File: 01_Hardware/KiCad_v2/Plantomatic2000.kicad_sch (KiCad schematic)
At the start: 256 parts, among them J101 Conn_02x05_Odd_Even, J102 Conn_02x03_Odd_Even, J103 USB_C_Receptacle_USB2.0_16P, J105 JST_B4B, J106 JST_B2B, J107 JST_B2B, J108 JST_B2B, J109 JST_B2B, J110 JST_B4B, J111 JST_B2B, J112 JST_B2B, J113 JST_B2B, J114 JST_B2B, J115 JST_B2B, J117 JST_B2B, Q101 STN3NF06L, Q102 STN3NF06L, Q103 UNH3N, Q104 BSS314PE, Q105 BSS314PE, Q106 BSS314PE, Q107 BSS314PE, Q108 NVTA7002NT1G, Q109 NVTA7002NT1G, Q110 NVTA7002NT1G, Q111 DMP6050SSD, Q112 DMP6050SSD, Q113 SI7615DN-T1-GE3, Q114 SI7615DN-T1-GE3, Q115 NVTA7002NT1G, Q116 NVTA7002NT1G, Q117 NVTA7002NT1G, SW102 SW_Push, SW103 SW_Push, U100 TLV61048, U101 XC6220B331MR, U102 BDJ2FC0WFP, U103 ESP32-WROOM-32E, U104 CYPD3177-24LQ, U105 USBLC6-2P6, U106 CP2102N-A02-GQFN24, U107 DS3231M, U108 AT24CS01-SSHM, U109 NCP1117-12_SOT223, U110 BQ25892, U111 XC6220B331MR

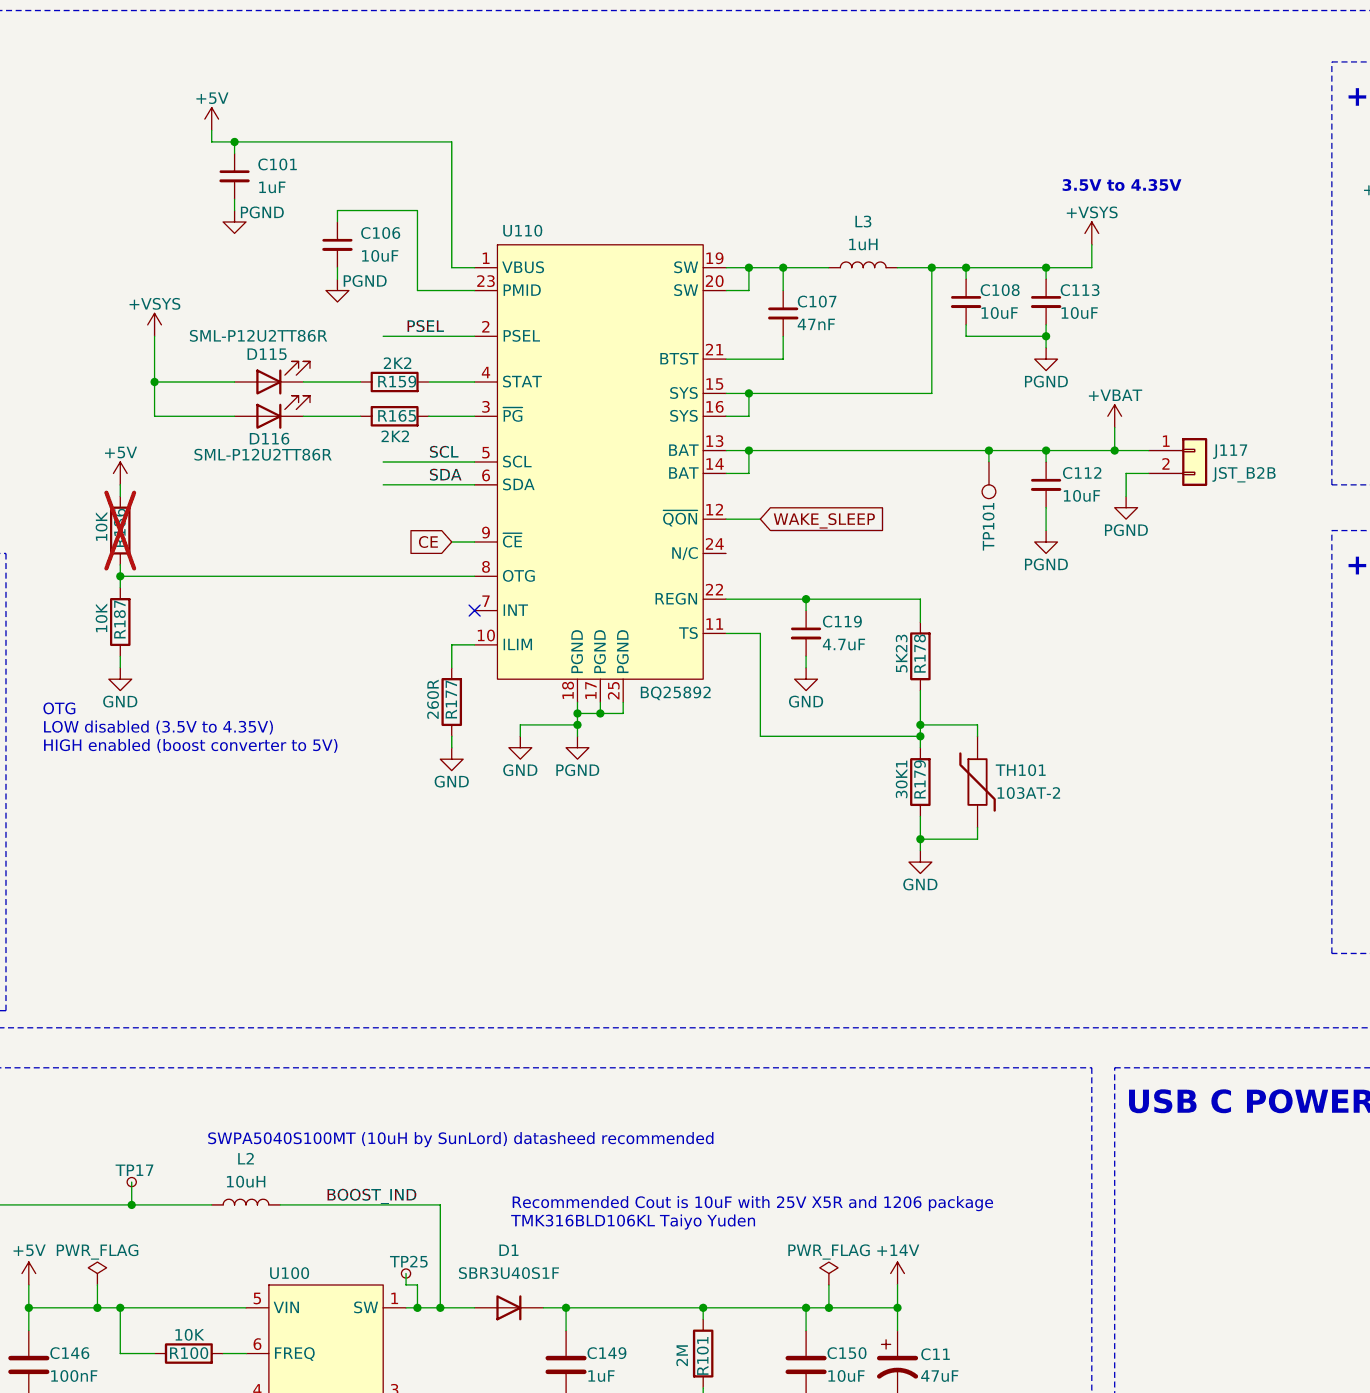
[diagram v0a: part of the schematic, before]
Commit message: Added footrpints for inductors and boost convereter
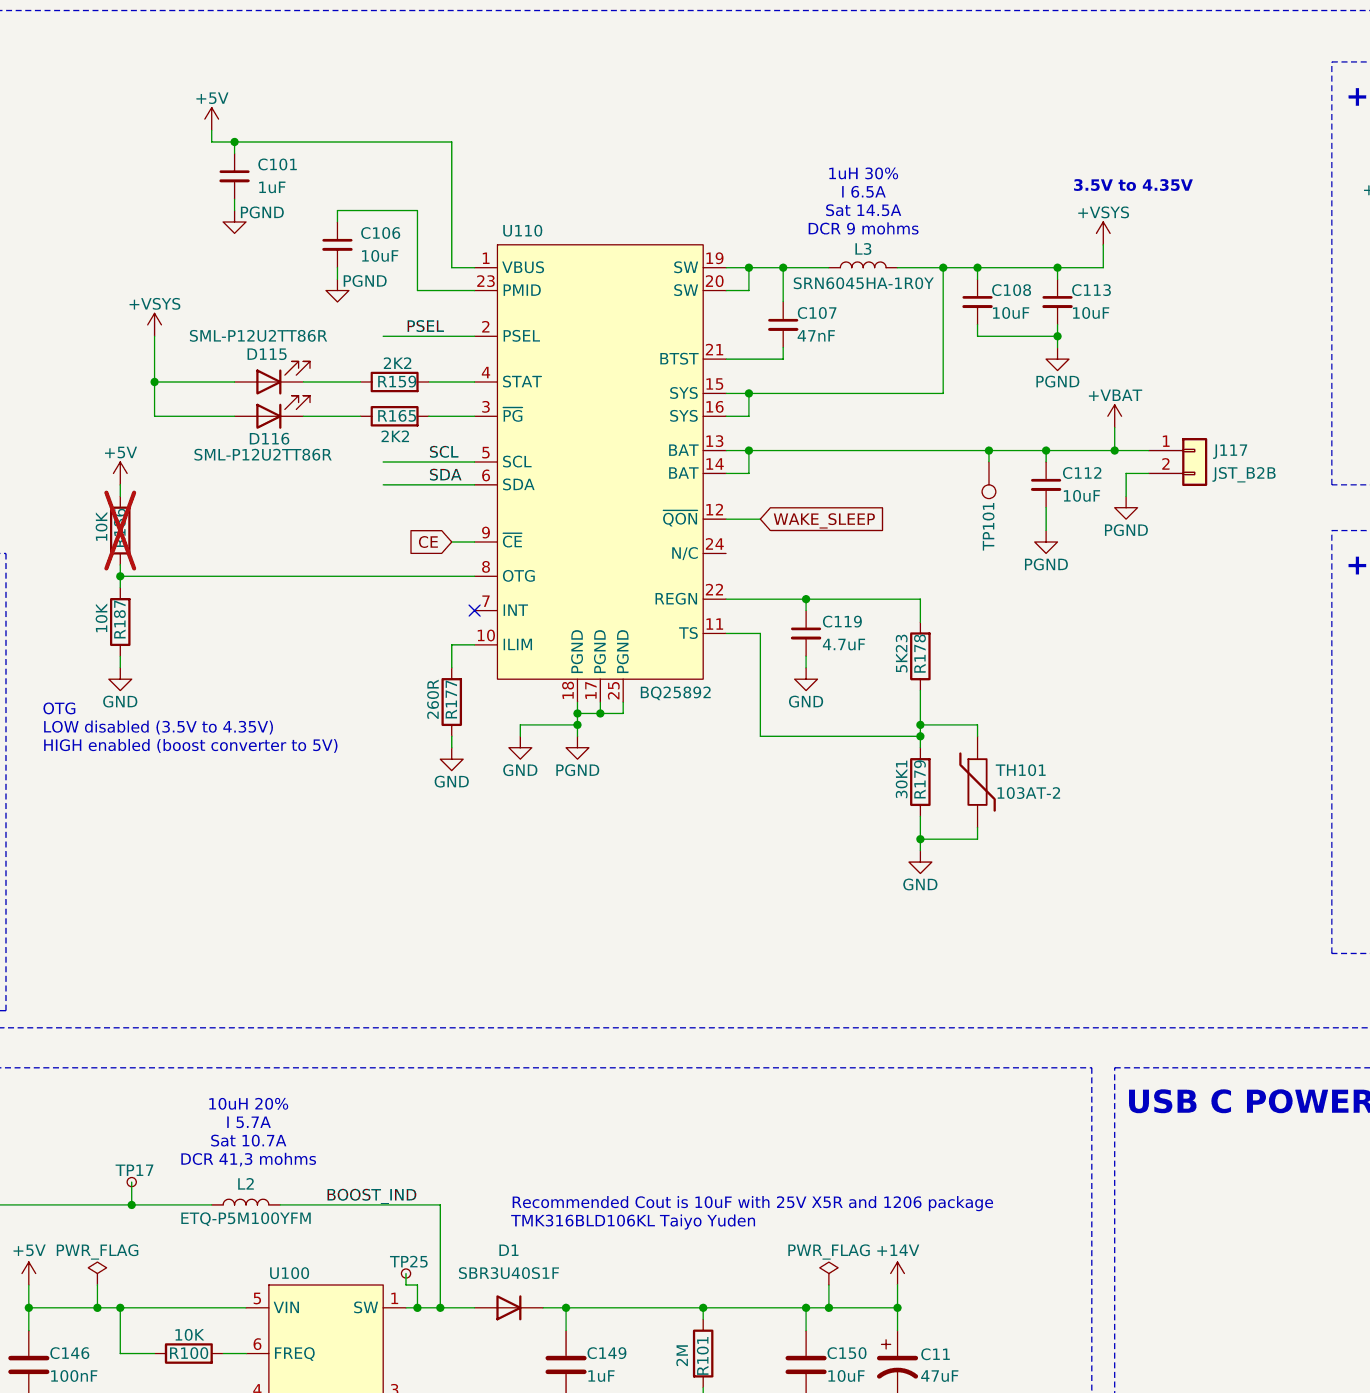
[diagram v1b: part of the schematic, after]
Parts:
- L2: value 10uH -> ETQ-P5M100YFM; footprint Custom_footprint:SWPA5040S -> Custom_Global_Footprints:ETQ-P5M100YFM
- L3: value 1uH -> SRN6045HA-1R0Y; footprint Custom_footprint:SWPA5040S -> Custom_Global_Footprints:SRN6045HA-1R0Y
- U100: footprint Custom_footprint:TLV61048 -> Custom_Global_Footprints:TLV61048
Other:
- note added: "10uH 20% I 5.7A Sat 10.7A DCR 41,3 mohms"
- note added: "1uH 30% I 6.5A Sat 14.5A DCR 9 mohms"
- note removed: "SWPA5040S100MT (10uH by SunLord) datasheed recommended"
- moved on the sheet: C107, C108, C113

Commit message: Checked footprints of diodes, resistors and BJT's
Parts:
- removed D103, D112, D113: SML-P12U2TT86R, LED_SMD:LED_0402_1005Metric, symbol Device:LED
- removed D106: 1N4148W, Diode_SMD:D_SOD-123, symbol Diode:1N4148W
- removed D3, D4: SBR3U40S1F, Diode_SMD:Nexperia_CFP3_SOD-123W, symbol Device:D
- removed R163: 10K, Resistor_SMD:R_0402_1005Metric, symbol Device:R
- added D107, D110: SML-P13PTT86R, LED_SMD:LED_0402_1005Metric, symbol Device:LED
- added D109, D112, D113: SBR3U40S1F, Custom_Global_Footprints:SBR3U40S1F-7, symbol Device:D
- added D115, D117: SML-P12U2TT86R, LED_SMD:LED_0402_1005Metric, symbol Device:LED
- added R184, R185: 4K7, Resistor_SMD:R_0402_1005Metric, symbol Device:R
- D101: renamed from D115; value SML-P12U2TT86R -> SML-P13PTT86R
- D104, D111: value SML-P12U2TT86R -> SML-P13PTT86R
- D105: renamed from D2; footprint Diode_SMD:Nexperia_CFP3_SOD-123W -> Custom_Global_Footprints:SBR3U40S1F-7
- D106: renamed from D1; footprint Diode_SMD:Nexperia_CFP3_SOD-123W -> Custom_Global_Footprints:SBR3U40S1F-7
- Q112: renamed from Q103; footprint (none) -> Package_TO_SOT_SMD:SOT-363_SC-70-6
- R102: renamed from R123; value 10K -> 1K
- R104: renamed from R159; value 2K2 -> 1K
- R106: renamed from R165; value 2K2 -> 1K
- R114: renamed from R176; value 10K -> 1K
- R136: renamed from R110; value 4K7 -> 1K
- R145: renamed from R119; value 1K -> 220R
- R146: renamed from R120; value 1K -> 220R
- R167: renamed from R161; value 1K -> 4K7
- renumbered BT101 to BT100, C102 to C100, C103 to C101, C104 to C102, C105 to C103, C101 to C104, C106 to C105, C148 to C106, C109 to C107, C111 to C108, C110 to C109, C147 to C110, C108 to C111, C113 to C112, C107 to C113, C112 to C114, C119 to C115, C166 to C116, C120 to C117, C121 to C118, C167 to C119, C115 to C120, C100 to C121, C116 to C122, C118 to C123, C117 to C124, C161 to C125, C160 to C126, C146 to C127, C149 to C128, C150 to C129, C11 to C130, C155 to C131, C156 to C132, C157 to C133, C158 to C134, C159 to C135, C128 to C136, C129 to C137, C130 to C138, C131 to C139, C132 to C140, C162 to C141, C163 to C142, C164 to C143, C165 to C144, C13 to C145, C151 to C146, C152 to C147, C153 to C148, C154 to C149, C12 to C150, C134 to C151, C135 to C152, C138 to C153, C139 to C154, C140 to C155, C141 to C156, C142 to C157, C143 to C158, C133 to C159, C137 to C160, C136 to C161, C144 to C162, C145 to C163, C114 to C164, D107 to D100, D116 to D102, D108 to D103, D117 to D108, H101 to H100, H102 to H101, H103 to H102, H104 to H103, H105 to H104, H106 to H105, J117 to J100, J114 to J104, J106 to J105, J107 to J106, J108 to J107, J109 to J108, J111 to J109, J115 to J110, J113 to J111, J110 to J112, J105 to J113, J112 to J114, L3 to L100, L2 to L101, Q117 to Q100, Q104 to Q101, Q113 to Q102, Q114 to Q103, Q106 to Q104, Q112 to Q105, Q111 to Q105, Q116 to Q106, Q115 to Q107, Q101 to Q108, Q110 to Q109, Q107 to Q110, Q105 to Q111, Q109 to Q113, Q108 to Q114, Q102 to Q115, R154 to R100, R150 to R101, R149 to R103, R164 to R105, R148 to R107, R186 to R108, R104 to R109, R187 to R110, R144 to R111, R145 to R112, R178 to R113, R177 to R115, R146 to R116, R179 to R117, R181 to R118, R183 to R119, R182 to R120, R156 to R121, R107 to R122, R143 to R123, R100 to R124, R101 to R125, R155 to R126, R160 to R127, R132 to R129, R166 to R130, R133 to R131, R131 to R132, R121 to R134, R130 to R135, R112 to R137, R111 to R138, R113 to R139, R114 to R140, R108 to R141, R115 to R142, R109 to R143, R117 to R144, R167 to R147, R169 to R148, R171 to R149, R173 to R150, R168 to R151, R170 to R152, R172 to R153, R174 to R154, R175 to R155, R134 to R156, R135 to R157, R136 to R158, R137 to R159, R138 to R160, R147 to R161, R139 to R162, R122 to R163, R102 to R164, R103 to R165, R125 to R166, R157 to R168, R162 to R169, R158 to R170, R124 to R171, R129 to R172, R142 to R173, R153 to R174, R152 to R175, R151 to R176, R127 to R177, R141 to R178, R105 to R179, R126 to R180, R140 to R181, R106 to R182, SW102 to SW100, SW103 to SW101, TH101 to TH100, TP103 to TP100, TP130 to TP101, TP128 to TP102, TP101 to TP103, TP114 to TP104, TP117 to TP105, TP118 to TP106, TP17 to TP107, TP25 to TP108, TP137 to TP109, TP15 to TP110, TP126 to TP111, TP116 to TP112, TP127 to TP113, TP115 to TP114, TP28 to TP115, TP29 to TP116, TP26 to TP117, TP27 to TP118, TP132 to TP119, TP133 to TP120, TP134 to TP121, TP135 to TP122, TP136 to TP123, TP131 to TP124, TP104 to TP125, TP107 to TP126, TP108 to TP127, TP109 to TP128, TP113 to TP129, TP111 to TP130, TP105 to TP131, TP112 to TP132, TP110 to TP133, TP106 to TP134, U101 to U100, U110 to U101, U103 to U102, U111 to U103, U100 to U104, U104 to U105, U102 to U106, U105 to U107, U106 to U108, U107 to U110, U108 to U111
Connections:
- net +12V_PUMP: now also D112.1 (K), D113.1 (K), R184.1
- net +12V_WATER: now also R185.1
- net +5V: now also R136.1; no longer D108.2 (A)
- net GND: now also D104.1 (K), D107.1 (K), D115.1 (K), D117.1 (K); no longer D111.1 (K)
- net LED_RX: now also D110.1 (K); no longer D104.1 (K)
- net LED_TX: now also D111.1 (K)
- net at D114.2 (A): now also R167.1
- net at C164.2, J114.1 (Pin_1), Q115.2 (D)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: now also D113.2 (A)
- net at R145.2: now also D111.2 (A)
- net at R163.1: now also D109.2 (A)
- net at C159.2, J111.1 (Pin_1), Q108.2 (D)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: now also D112.2 (A)
- net at D104.2 (A): now also R119.1; no longer R146.2
- net at D118.2 (A): now also R185.2; no longer R119.1
- net at D108.1 (K): now also Q107.3 (D); no longer R136.1
- net at R127.1: now also D107.2 (A); no longer D111.2 (A)
- net at R169.1: now also D115.2 (A)
- net at BT100.1 (+), U110.14 (VBAT): now also D109.1 (K)
- net at R136.2: now also D108.2 (A); no longer Q107.3 (D)
- new net: D117.2 (A), R184.2
- new net: D110.2 (A), R146.2
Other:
- note added: "GREEN"
- note added: "RED"
- moved on the sheet: C141, C142, C143, C144, C145, C146, C147, C148, C149, C150, D108, R136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

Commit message: Schematic annotated, net labes, some values consolidated
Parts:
- removed C119, C120, C155, C157, C158, C161: 100nF, Capacitor_SMD:C_0402_1005Metric, symbol Device:C_Small
- removed C121, C128: 1uF, Capacitor_SMD:C_0603_1608Metric, symbol Device:C
- removed C127: 100nF, Capacitor_SMD:C_0402_1005Metric, symbol Device:C
- removed C129, C141, C143, C146, C148: 10uF, Capacitor_SMD:C_0603_1608Metric, symbol Device:C
- removed C130, C145, C150: 47uF, Capacitor_SMD:CP_Elec_6.3x7.7, symbol Device:C_Polarized_US
- removed C142, C144, C147, C149: 10nF, Capacitor_SMD:C_0402_1005Metric, symbol Device:C
- removed D108: SML-P12U2TT86R, LED_SMD:LED_0402_1005Metric, symbol Device:LED
- removed R103, R121: 470R, Resistor_SMD:R_0402_1005Metric, symbol Device:R
- removed R104, R119, R169: 1K, Resistor_SMD:R_0402_1005Metric, symbol Device:R
- removed R108, R109, R124, R153: 10K, Resistor_SMD:R_0402_1005Metric, symbol Device:R
- removed R118: 22K, Resistor_SMD:R_0402_1005Metric, symbol Device:R
- removed R143: 4K7, Resistor_SMD:R_0402_1005Metric, symbol Device:R
- added C104, C175, C176, C177: 100nF, Capacitor_SMD:C_0603_1608Metric, symbol Device:C_Small
- added C119, C161: 47uF, Capacitor_SMD:C_0402_1005Metric, symbol Device:C_Polarized_Small
- added C120, C136, C158: 47uF, Capacitor_SMD:C_0603_1608Metric, symbol Device:C_Polarized_Small
- added C121: 47nF, Capacitor_SMD:C_0603_1608Metric, symbol Device:C_Small
- added C127, C144, C165: 10uF, Capacitor_SMD:C_0402_1005Metric, symbol Device:C_Small
- added C128: 4.7uF, Capacitor_SMD:C_0402_1005Metric, symbol Device:C_Small
- added C129, C130, C142, C147, C166, C167, C168, C169, C170, C171, C172, C173, C174: 100nF, Capacitor_SMD:C_0402_1005Metric, symbol Device:C_Small
- added C141, C145: 47uF, Capacitor_SMD:CP_Elec_6.3x5.8, symbol Device:C_Polarized_Small
- added C143: 1uF, Capacitor_SMD:C_0603_1608Metric, symbol Device:C_Small
- added C149: 10uF, Capacitor_SMD:C_0402_1005Metric, symbol Device:C_Polarized_Small
- added C150: 10uF, Capacitor_SMD:C_1206_3216Metric, symbol Device:C_Polarized_Small
- added C155: 220uF, Capacitor_SMD:CP_Elec_10x10, symbol Device:C_Polarized_US
- added C157: 220uF, Capacitor_SMD:C_0603_1608Metric, symbol Device:C_Polarized_US
- added D104: SML-P12U2TT86R, LED_SMD:LED_0402_1005Metric, symbol Device:LED
- added R111, R125, R128: 10K, Resistor_SMD:R_0402_1005Metric, symbol Device:R
- added R113, R117: 1K, Resistor_SMD:R_0402_1005Metric, symbol Device:R
- added R133, R151, R155, R177, R183: 0R, Resistor_SMD:R_0402_1005Metric, symbol Device:R
- added R137: 470R, Resistor_SMD:R_0402_1005Metric, symbol Device:R
- added R139: 4K7, Resistor_SMD:R_0402_1005Metric, symbol Device:R
- added R145: 22K1, Resistor_SMD:R_0402_1005Metric, symbol Device:R
- C100: renamed from C136; footprint Capacitor_SMD:C_0603_1608Metric -> Capacitor_SMD:C_0402_1005Metric
- C101: value 10uF tantulum -> 100nF
- C102: renamed from C104; footprint (none) -> Capacitor_SMD:C_0603_1608Metric
- C103: value 100nF -> 10uF; now fitted
- C105: value 10uF -> 8.2uF; footprint (none) -> Capacitor_SMD:C_0603_1608Metric
- C107, C117, C118: footprint Capacitor_SMD:C_0603_1608Metric -> Capacitor_SMD:CP_Elec_6.3x5.8
- C108: value 1uF -> 10uF; footprint Capacitor_SMD:C_0402_1005Metric -> Capacitor_SMD:C_0603_1608Metric
- C109: value 10uF -> 100nF; footprint Capacitor_SMD:C_0603_1608Metric -> Capacitor_SMD:CP_Elec_6.3x5.8
- C111: footprint (none) -> Capacitor_SMD:C_1206_3216Metric
- C112: value 10uF -> 4.7uF; footprint (none) -> Capacitor_SMD:CP_Elec_6.3x5.8
- C113: value 47nF -> 100nF; footprint (none) -> Capacitor_SMD:CP_Elec_6.3x5.8
- C114: value 10uF -> 4.7uF; footprint Capacitor_SMD:C_0402_1005Metric -> Capacitor_SMD:CP_Elec_6.3x5.8
- C115: value 4.7uF -> 1uF; footprint Capacitor_SMD:C_0402_1005Metric -> Capacitor_SMD:C_0603_1608Metric
- C116, C151: value 100nF -> 1uF
- C122: value 100nF -> 1uF; footprint Capacitor_SMD:C_0402_1005Metric -> Capacitor_SMD:C_0603_1608Metric
- C123, C124, C125, C153, C156, C162: footprint Capacitor_SMD:C_0402_1005Metric -> Capacitor_SMD:C_0603_1608Metric
- C126, C134, C164: value 1uF -> 100nF
- C131: value 10uF -> 1uF
- C132, C137, C140, C152: value 100nF -> 10uF
- C135: value 3.3uF -> 10uF
- C139: value 4.7uF -> 100nF
- C146: renamed from C102; footprint Capacitor_SMD:C_0603_1608Metric -> Capacitor_SMD:CP_Elec_10x10
- C148: renamed from C100; value 100nF tantulum -> 100nF; footprint Capacitor_SMD:C_1206_3216Metric -> Capacitor_SMD:CP_Elec_10x10
- C159: value 1uF -> 10uF
- C160: value 10uF -> 100nF; footprint Capacitor_SMD:C_0402_1005Metric -> Capacitor_SMD:C_0603_1608Metric
- D105: renamed from D111; footprint LED_SMD:LED_0402_1005Metric -> Custom_Global_Footprints:SBR3U40S1F-7
- D106: renamed from D110; footprint LED_SMD:LED_0402_1005Metric -> Custom_Global_Footprints:SBR3U40S1F-7
- D112: renamed from D107; footprint LED_SMD:LED_0402_1005Metric -> Custom_Global_Footprints:SBR3U40S1F-7
- D114: renamed from D113; footprint Custom_Global_Footprints:SBR3U40S1F-7 -> LED_SMD:LED_0402_1005Metric
- D115: renamed from D112; footprint Custom_Global_Footprints:SBR3U40S1F-7 -> LED_SMD:LED_0402_1005Metric
- J101: renamed from J103; footprint Connector_USB:USB_C_Receptacle_Palconn_UTC16-G -> Connector_PinHeader_1.27mm:PinHeader_2x05_P1.27mm_Vertical_SMD
- J102: renamed from J112; footprint Connector_JST:JST_EH_B4B-EH-A_1x04_P2.50mm_Vertical -> Connector_PinHeader_1.27mm:PinHeader_2x03_P1.27mm_Vertical_SMD
- J103: renamed from J113; footprint Connector_JST:JST_EH_B4B-EH-A_1x04_P2.50mm_Vertical -> Connector_USB:USB_C_Receptacle_Palconn_UTC16-G
- J106: renamed from J101; footprint Connector_PinHeader_1.27mm:PinHeader_2x05_P1.27mm_Vertical_SMD -> Connector_JST:JST_EH_B2B-EH-A_1x02_P2.50mm_Vertical
- J107: renamed from J102; footprint Connector_PinHeader_1.27mm:PinHeader_2x03_P1.27mm_Vertical_SMD -> Connector_JST:JST_EH_B2B-EH-A_1x02_P2.50mm_Vertical
- J112: renamed from J108; footprint Connector_JST:JST_EH_B2B-EH-A_1x02_P2.50mm_Vertical -> Connector_JST:JST_EH_B4B-EH-A_1x04_P2.50mm_Vertical
- J113: renamed from J109; footprint Connector_JST:JST_EH_B2B-EH-A_1x02_P2.50mm_Vertical -> Connector_JST:JST_EH_B4B-EH-A_1x04_P2.50mm_Vertical
- Q100: renamed from Q102; footprint Package_SON:Diodes_PowerDI3333-8 -> Custom_Global_Footprints:NVTA7002N
- Q101: renamed from Q103; footprint Package_SON:Diodes_PowerDI3333-8 -> Custom_Global_Footprints:BSS314PE
- Q102: renamed from Q105; footprint Package_SO:SOIC-8_3.9x4.9mm_P1.27mm -> Package_SON:Diodes_PowerDI3333-8
- Q103: renamed from Q112; footprint Package_TO_SOT_SMD:SOT-363_SC-70-6 -> Package_SON:Diodes_PowerDI3333-8
- Q104: renamed from Q107; footprint Custom_Global_Footprints:NVTA7002N -> Custom_Global_Footprints:BSS314PE
- Q105: renamed from Q101; footprint Custom_Global_Footprints:BSS314PE -> Package_SO:SOIC-8_3.9x4.9mm_P1.27mm
- Q107: renamed from Q104; footprint Custom_Global_Footprints:BSS314PE -> Custom_Global_Footprints:NVTA7002N
- Q108: renamed from Q106; footprint Custom_Global_Footprints:NVTA7002N -> Package_TO_SOT_SMD:SOT-223
- Q109: renamed from Q110; footprint Custom_Global_Footprints:BSS314PE -> Custom_Global_Footprints:NVTA7002N
- Q111: renamed from Q115; footprint Package_TO_SOT_SMD:SOT-223 -> Custom_Global_Footprints:BSS314PE
- Q112: renamed from Q108; footprint Package_TO_SOT_SMD:SOT-223 -> Package_TO_SOT_SMD:SOT-363_SC-70-6
- Q115: renamed from Q109; footprint Custom_Global_Footprints:NVTA7002N -> Package_TO_SOT_SMD:SOT-223
- R100, R101, R107, R135: value 10K -> 1K
- R102, R114, R136: value 1K -> 10K
- R105: value 0R -> 1K
- R106, R127, R131, R156: value 1K -> 0R
- R110, R180, R181, R182: value 10K -> 0R
- R112, R185: value 4K7 -> 1K
- R116: value 0R -> 220R
- R119: renamed from R115; value 260R -> 130R
- R120, R173: value 10K -> 470R
- R122, R164: value 470R -> 4K7
- R126: value 22K -> 10K; now not fitted
- R132: value 470R -> 10K; now not fitted
- R134, R161: value 1K -> 22K1
- R138: value 220R -> 10K
- R140, R149, R152: value 0R -> 10K
- R141, R174, R175, R176: value 4K7 -> 10K
- R142, R154: value 0R -> 4K7
- R143: renamed from R125; value 2M -> 1M
- R144: renamed from R128; value 121K -> 64K9
- R146: value 220R -> 1K
- R147, R150: now fitted
- R148: value 10K -> 470R; now fitted
- R157: value 1K -> 220R
- R158, R159, R160: value 1K -> 4K7
- R163: value 220R -> 22K1
- R166: value 470R -> 10K
- R167: value 4K7 -> 470R
- R168, R170: value 22K -> 470R
- R178, R179: value 470R -> 0R
- R184: value 4K7 -> 0R
- U101: renamed from U103; footprint Package_TO_SOT_SMD:SOT-23-5 -> Package_DFN_QFN:WQFN-24-1EP_4x4mm_P0.5mm_EP2.45x2.45mm_ThermalVias
- U102: renamed from U101; footprint Package_DFN_QFN:WQFN-24-1EP_4x4mm_P0.5mm_EP2.45x2.45mm_ThermalVias -> RF_Module:ESP32-WROOM-32E
- U103: renamed from U107; footprint Package_TO_SOT_SMD:SOT-666 -> Package_TO_SOT_SMD:SOT-23-5
- U104: renamed from U108; footprint Package_DFN_QFN:QFN-24-1EP_4x4mm_P0.5mm_EP2.7x2.6mm_ThermalVias -> Custom_Global_Footprints:TLV61048
- U106: renamed from U109; footprint Package_TO_SOT_SMD:SOT-223-3_TabPin2 -> Package_TO_SOT_SMD:TO-252-5_TabPin3
- U107: renamed from U106; footprint Package_TO_SOT_SMD:TO-252-5_TabPin3 -> Package_TO_SOT_SMD:SOT-666
- U108: renamed from U104; footprint Custom_Global_Footprints:TLV61048 -> Package_DFN_QFN:QFN-24-1EP_4x4mm_P0.5mm_EP2.7x2.6mm_ThermalVias
- U109: renamed from U102; footprint RF_Module:ESP32-WROOM-32E -> Package_TO_SOT_SMD:SOT-223-3_TabPin2
- U110: renamed from U111; footprint Package_SO:SOIC-8_3.9x4.9mm_P1.27mm -> Package_SO:SOIC-16W_7.5x10.3mm_P1.27mm
- U111: renamed from U110; footprint Package_SO:SOIC-16W_7.5x10.3mm_P1.27mm -> Package_SO:SOIC-8_3.9x4.9mm_P1.27mm
- renumbered D103 to D101, D101 to D102, D102 to D103, D104 to D107, D105 to D108, D106 to D109, D117 to D110, D118 to D111, D109 to D113, D114 to D116, D115 to D117, J114 to J104, J111 to J105, J104 to J108, J105 to J109, J106 to J110, J107 to J111, J110 to J114, Q100 to Q106, Q111 to Q110, R139 to R103, R137 to R104, R130 to R108, R144 to R109, R145 to R115, R113 to R118, R117 to R121, R155 to R124, R151 to R130, R111 to R153, R177 to R169, TP104 to TP101, TP112 to TP102, TP114 to TP103, TP103 to TP104, TP102 to TP105, TP107 to TP106, TP117 to TP107, TP118 to TP108, TP108 to TP109, TP115 to TP110, TP116 to TP111, TP110 to TP112, TP109 to TP113, TP111 to TP114, TP113 to TP115, TP101 to TP116, TP105 to TP117, TP106 to TP118, TP128 to TP119, TP129 to TP120, TP130 to TP121, TP131 to TP122, TP125 to TP123, TP132 to TP124, TP134 to TP125, TP133 to TP126, TP126 to TP127, TP127 to TP128, TP119 to TP129, TP120 to TP130, TP121 to TP131, TP122 to TP132, TP123 to TP133, TP124 to TP134
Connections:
- net PMIC_SHPHLD is gone; now on net WAKE_SLEEP: Q115.3 (D)
- net +12V_PUMP: now also C139.1, C140.1, C154.1, C156.1, C141.1, C155.1, C157.1, C167.1, R139.1; no longer C159.1, R184.1
- net +12V_WATER: now also C134.1, C135.1, C162.1, C163.1, R142.1, R166.2, C136.1, C161.1; no longer R173.2, R185.1
- net +3V3: now also C110.1, C111.1, C152.1, C153.1, C159.1, R101.1, R150.1, R152.2, R154.1, R157.1, R158.1, R159.1, R160.1, R165.2, R185.1, C147.1, C149.1, C150.1, C158.1, C165.1, C166.1; no longer C101.1, C103.1, C118.1, C162.1, C163.1, R100.1, R112.1, R114.2, R162.2, R163.2, R172.2, R174.1, R175.1, R176.1
- net +3V3_MCU: now also C106.1, C107.1, R100.1; no longer C109.1, C110.1, R102.2
- net +5V: now also C116.1, R136.2, R140.2, C142.1, R111.1, R113.1; no longer C126.1, R120.2, R136.1
- net +VBAT: now also C127.1; no longer C114.1
- net +VBUS: now also C101.1, C112.1, C115.1, C126.1, J106.1 (Pin_1), J107.2 (Pin_2), R102.1, C168.1, C169.1; no longer C125.1, C135.1, C137.1, C140.1, R123.1
- net +VDD: now also C113.1, C114.1, R116.1; no longer C138.1, C139.1, R146.1
- net +VDDD: now also C122.1, C123.1, C124.1, R122.1, R126.1, R127.1, R125.1, R128.1; no longer C131.1, C132.1, C133.1, R141.1, R147.1, R148.1, R149.1, R150.1
- net +VSYS: now also C103.1, C108.1, C109.1, C118.1, R129.1, R147.2, C104.1, C119.1, C120.1; no longer C106.1, C107.1, C111.1, C112.1, C116.1, R101.2, R129.2
- net BOOST_ENABLE: now also R148.1, R149.1; no longer R132.1, R135.2
- net CE: now also R129.2; no longer R101.1
- net CHARGE_ENABLE: now also R138.1, R137.1; no longer R107.2
- net DISPLAY_ENABLE: now also R175.1; no longer R180.2
- net ESP_EN: now also C151.1, R150.2, R184.1; no longer C108.1, R100.2, R122.1
- net ESP_IO0: now also R183.1
- net ESP_RX: now also R106.1; no longer R140.2
- net ESP_TX: now also R110.1, R151.1; no longer R105.2, R142.2
- net GND: now also C113.2, C125.2, C126.2, C159.2, R114.2, R123.2, R131.2, R132.2, R134.2, R138.2, R149.2, R161.2, R163.2, R171.2, R172.2, R174.2, R175.2, R176.2, C104.2, C119.2, C120.2, C127.2, C128.2, C129.2, C130.2, C136.2, C141.2, C142.2, C143.2, C144.2, C145.2, C147.2, C149.2, C150.2, C155.2, C157.2, C158.2, C161.2, C165.2, C166.2, C168.2, C169.2, C170.2, C171.2, C172.2, C173.2, C174.2, C175.2, C176.2, C177.2, R133.2, R145.2; no longer C115.2, C116.2, R107.1, R110.1, R126.1, R135.1, R152.2, R154.2, R165.1, R168.1, R170.1, R171.1, R180.1, R181.1, R182.1
- net HOUR_BUTTON_PIN: now also R180.1; no longer R159.2
- net ISNK_COARSE: now also R127.2, R132.1; no longer R149.2
- net ISNK_FINE: now also R128.2, R133.1; no longer R150.2, R154.1
- net MIN_BUTTON_PIN: now also R181.1; no longer R160.2
- net PSEL: now also R134.1, R135.1
- net PUMP1_EN: now also R168.1, R171.1; no longer R164.1, R165.2
- net PUMP2_EN: now also R167.1, R172.1; no longer R179.1, R182.2
- net RESET_BUTTON_PIN: now also R182.1; no longer R161.2
- net SELECT_LINE_BUTTON_PIN: now also R178.1; no longer R157.2
- net SER_RX: now also R110.2; no longer R142.1
- net SER_TX: now also R106.2; no longer R140.1
- net START_BUTTON_PIN: now also R179.1; no longer R158.2
- net VBUS_FET_SAFE_EN: now also R136.1, R117.1; no longer R120.1, R134.2
- net VBUS_MAX: now also R125.2; no longer R147.2
- net VBUS_MIN: now also R126.2, R131.1; no longer R148.2, R152.1
- net WAKE_SLEEP: now also R177.1; no longer R156.2
- net WATER_SENSOR_EN: now also R170.1, R174.1; no longer R178.1, R181.2
- net at J102.1 (Pin_1), Q110.3 (D), TP119.1: now also R163.1, R164.1; no longer R167.2, R170.2
- net at J113.2 (Pin_2), TP133.1: now also R182.2, C175.1; no longer R161.1
- net at J114.2 (Pin_2): now also R185.2; no longer R162.1
- net at J101.S1 (SHIELD), R124.1: now also C129.1, C130.1; no longer C151.1, C152.1
- net at D107.2 (A): now also R135.2
- net at Q106.1 (G), TP105.1: now also R137.2
- net at J109.2 (Pin_2), TP129.1: now also R178.2, C171.1; no longer C154.1, R157.1
- net at Q114.1 (G), TP126.1: now also R170.2; no longer R178.2
- net at Q110.1 (G), Q114.3 (D), TP121.1: now also R166.1; no longer R173.1
- net at Q109.1 (G), Q113.3 (D), TP120.1: now also R165.1; no longer R172.1
- net at D117.2 (A): now also R162.2
- net at D111.2 (A): now also R142.2; no longer R185.2
- net TS: now reaches R118.1, R121.2, TH100.1, U102.11 (TS)
- net at D108.1 (K), L101.1, TP106.1: now also C131.1
- net at R184.2: now also SW101.2, C176.1; no longer D110.2 (A)
- net at D116.2 (A): now also R164.2; no longer R167.1
- net at J108.2 (Pin_2), TP134.1: now also C170.1, R177.2; no longer C153.1, R156.1
- net at D113.2 (A): now also R157.2; no longer R163.1
- net at U110.1 (A0): now also R160.2; no longer R176.2
- net at D115.2 (A), J105.1 (Pin_1), Q112.2 (D)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: now also C167.2; no longer C159.2
- net at D101.2 (A): now also R101.2; no longer R114.1
- net at D106.2 (A): now also R116.2; no longer R146.2
- net at J111.2 (Pin_2), TP131.1: now also R180.2, C173.1; no longer C156.1, R159.1
- net at L100.1, U102.19 (SW), U102.20 (SW): now also C121.1; no longer C113.1
- net at Q107.1 (G), Q108.3 (D), TP114.1: now also R147.1; no longer R129.1
- net at Q107.3 (D), TP113.1, U108.4 (EN): now also R146.1, R145.1; no longer R126.2, R127.2
- net at Q111.1 (G), TP125.1: now also R167.2; no longer R179.2
- net at Q104.3 (D): now also D104.1 (K)
- net FAULT: now reaches U105.9 (FAULT)
- net FAULT: now also R120.1, R123.1; no longer R138.1
- net at Q104.1 (G): now also R120.2; no longer R138.2
- net RST: now reaches R104.2, U104.9 (~{RST})
- net at J112.2 (Pin_2), TP132.1: now also R181.2, C174.1; no longer R160.1
- net at Q108.1 (G), TP115.1: now also R148.2; no longer R132.2
- net at Q112.1 (G), TP127.1: now also R168.2; no longer R164.2
- net at D112.2 (A): now also R146.2; no longer R127.1
- net at J110.2 (Pin_2), TP130.1: now also R179.2, C172.1; no longer R158.1
- net at U109.27 (IO16): now also R152.1
- net 3V3_DISPLAY: now reaches J103.2 (Pin_2), Q109.3 (D)
- net 3V3_DISPLAY: now also R161.1, R162.1; no longer R168.2
- net at Q115.1 (G), TP128.1: now also R173.2; no longer R166.2
- net at U105.4 (SAFE_PWR_EN): now also R117.2; no longer R134.1
- net at U109.33 (IO21): now also R155.2; no longer R116.1
- net at SW100.2: now also C177.1, R183.2; no longer C124.1
- net at U110.3 (A2): now also R158.2; no longer R174.2
- net at U108.6 (FREQ): now also R140.1
- net at D100.2 (A): now also R100.2; no longer R102.1
- net at D102.1 (K): now also R105.2
- net STAT: now reaches U102.4 (STAT)
- net STAT: now also R105.1
- net at U105.3 (VBUS_FET_EN): now also R112.2; no longer R131.1
- net at U110.2 (A1): now also R159.2; no longer R175.2
- net ESP_TXR: now reaches U109.35 (TXD0/IO1)
- net ESP_TXR: now also R151.2; no longer R105.1
- net at U105.10 (FLIP): now also R122.2; no longer R141.2
- net REGN: now reaches R118.2, U102.22 (REGN)
- net REGN: now also C128.1; no longer C115.1
- net VCCD: now reaches U105.24 (VCCD)
- net VCCD: now also C125.1; no longer C134.1
- net ILIM: now reaches R119.2, U102.10 (ILIM)
- net at U102.21 (BTST): now also C121.2; no longer C113.2
- net PG: now reaches U102.3 (~{PG})
- net PG: now also R107.1; no longer R106.2
- net OTG: now reaches U102.8 (OTG)
- net OTG: now also R114.1, R111.2; no longer R110.2
- net at D103.1 (K): now also R107.2; no longer R106.1
- net +14V renamed +13V
- net +13V: now also C132.1, C133.1, C137.1, C138.1, R141.1, C143.1, C144.1, C145.1; no longer U107.1 (EN)
- net SCL renamed ESP_SCL
- net ESP_SCL: now also R155.1; no longer R116.2
- net SDA renamed ESP_SDA
- net ESP_SDA: now also R154.2, R156.1; no longer R112.2, U109.36 (IO22)
- removed net VBUS: C122.1, J106.1 (Pin_1), J107.2 (Pin_2)
- new net: R141.2, U107.1 (EN)
- new net: R173.1, R176.1, U111.3 (~{INT}/SQW)
- new net: D104.2 (A), R113.2
- new net: R156.2, U109.36 (IO22)
- new net: D110.2 (A), R139.2
- new net VBUS_FET_EN: C115.2, C116.2, Q100.4 (G), Q101.4 (G), R102.2, R112.1
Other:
- note added: "+12V LDO PUMPS"
- note added: "+12V LDO WATER"
- note added: "+3V/+5.5V TO +13V BOOST CONVERTER"
- note added: "ERA-2AEB3012X"
- note added: "ERJ-2RKF6492X <- 1%"
- note added: "ILIM set to 3A max"
- note added: "Output Voltage: R2 should be kept under 150K as per datasheet R1=(Vout/Vref - 1) * R2 R1=[(13V/0.8V)-1] * 64K9 = 1M R1 = 1M R2 = 64K9K Vout = 13V"
- note added: "RE0402BRE071ML"
- note added: "RG1005P-131-B-T5"
- note added: "RGC1/16SC6492BTH"
- note added: "RT0402BRE075K23L"
- note added: "UUX1E221MNL1GS"
- note added: "UWT1V470MCL1GS"
- note removed: "+12V LDO"
- note removed: "+3V/+5.5V TO +14V BOOST CONVERTER"
- note removed: "Ceramic"
- note removed: "GREEN"
- note removed: "Output Voltage: R2 should be kept under 150K as per datasheet R1=(Vout/Vref - 1) * R2 R1=[(14V/0.8V)-1] * 121K = 2M R1 = 2M R2 = 121K Vout = 14V"
- note removed: "RED"
- note removed: "TO DO: Find suitable LED's REG / GREEN etc Fix the MOSFET pinout Find suitable capacitors ( correct foot print and voltage rating ) Re-Check schematic for correct values and symbos Re-Check and Re-Do PDN block diagram and check logic Check the BMU thermistor and resustir values Re-evaluate the sleep/wake logic between RTC / ESP32 / BQ25892 QON pin Check footrpints for all components Re-check pino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"
- moved on the sheet: BT100, C100, C102, C105, C146, C148, D100, D101, D102, D103, D105, D106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
